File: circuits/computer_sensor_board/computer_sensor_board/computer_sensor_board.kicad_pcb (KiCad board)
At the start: 2 copper layers, 70 x 35 mm, 13 parts, among them J1 Conn_Switching_Hub, J2 Conn_Jetson, J5 Conn_VLP16, J6 Conn_Main_DCDC, J7 Conn_Router

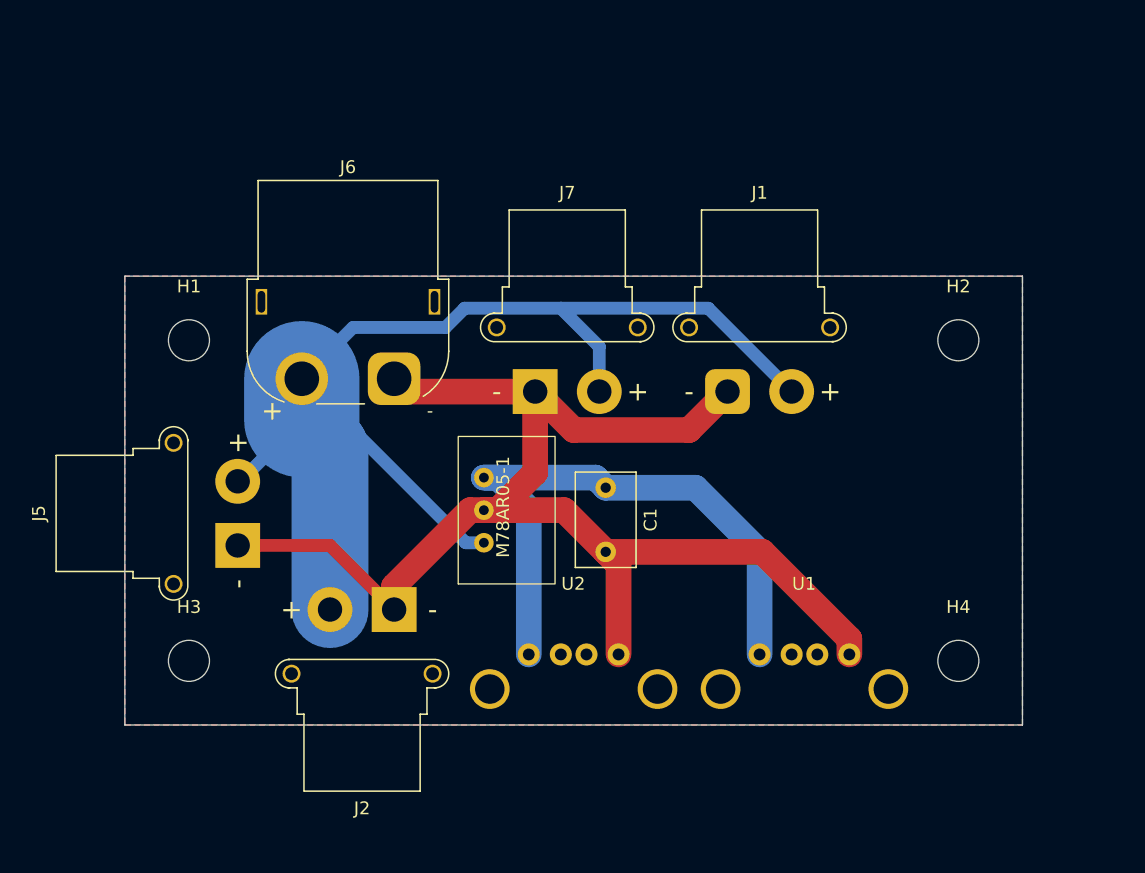
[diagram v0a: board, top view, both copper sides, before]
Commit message: change Pch MOSFET
Signed-off-by: Masaya Kataoka <ms.kataoka@gmail.com>
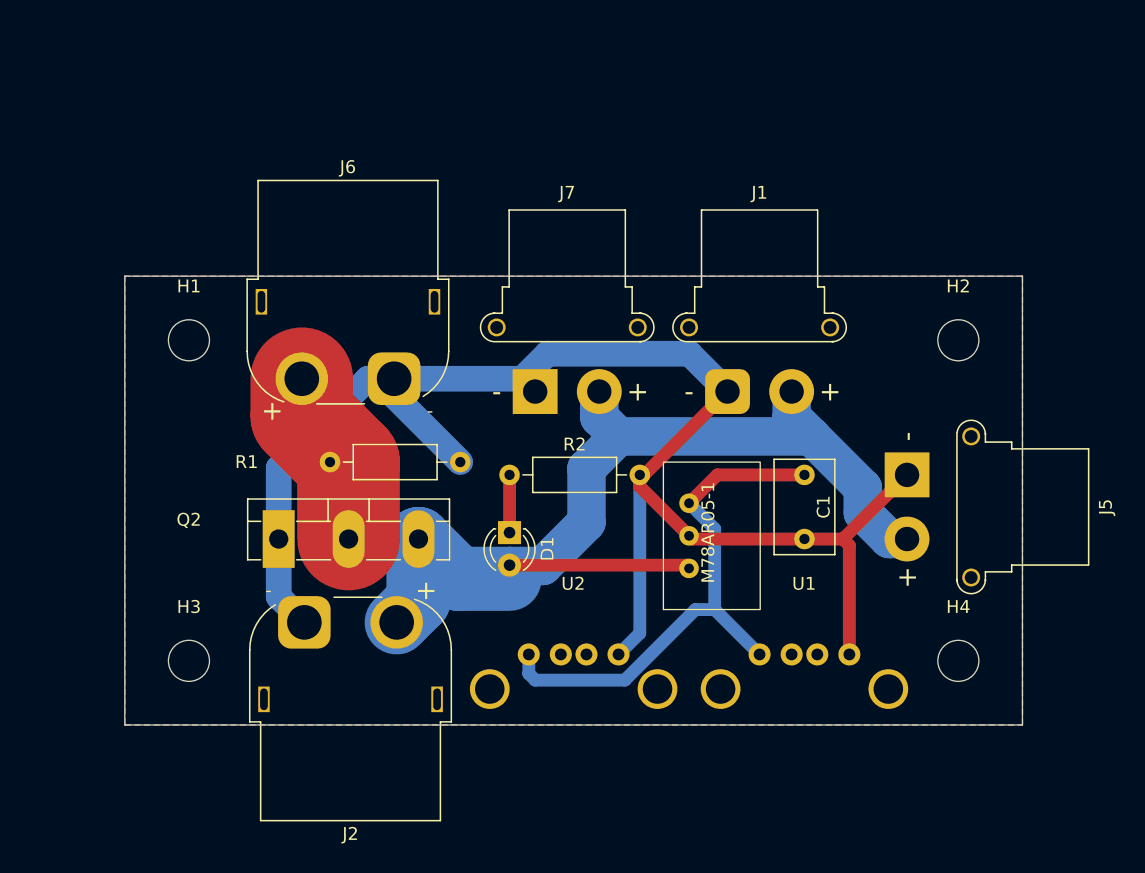
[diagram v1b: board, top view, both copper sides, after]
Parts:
- added D1: LED, LED_THT:LED_D3.0mm, F.Cu at (200.0, 75.0)
- added Q2: 2SJ555-E, Package_TO_SOT_THT:TO-3P-3_Vertical, F.Cu at (182.0, 75.5)
- added R1: 100K, Resistor_THT:R_Axial_DIN0207_L6.3mm_D2.5mm_P10.16mm_Horizontal, F.Cu at (186.0, 69.5)
- added R2: 390, Resistor_THT:R_Axial_DIN0207_L6.3mm_D2.5mm_P10.16mm_Horizontal, F.Cu at (200.0, 70.5)
- J2: footprint Connector_AMASS:AMASS_XT30PW-F_1x02_P2.50mm_Horizontal -> Connector_AMASS:AMASS_XT60PW-F_1x02_P7.20mm_Horizontal
- moved J5 52.5 mm to (231.0, 70.5), turned to -90 degrees
- moved M78AR05-1 16.1 mm to (216.0, 75.0)
- moved C1 15.5 mm to (223.0, 70.5)
- moved J2 7.07 mm to (184.0, 82.0)
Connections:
- J1 pad 2: Net-(J1-Pin_2) -> Net-(D1-A)
- J2 pad 2: Net-(J1-Pin_2) -> Net-(D1-A)
- J5 pad 2: Net-(J1-Pin_2) -> Net-(D1-A)
- J6 pad 2: Net-(J1-Pin_2) -> Net-(J6-Pin_2)
- J7 pad 2: Net-(J1-Pin_2) -> Net-(D1-A)
- M78AR05-1 pad 1: Net-(J1-Pin_2) -> Net-(D1-A)
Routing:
- net Net-(J1-Pin_2): track 96.3 -> 0.00 mm
- net Net-(D1-A): track 0.00 -> 80.0 mm
- net GND: track 108.3 -> 123.5 mm
- net Net-(J6-Pin_2): track 0.00 -> 14.0 mm
- net Net-(M78AR05-1-Vout): track 47.8 -> 42.5 mm
- net Net-(D1-K): track 0.00 -> 4.50 mm

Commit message: add heatsink
Signed-off-by: Masaya Kataoka <ms.kataoka@gmail.com>
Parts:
- added HS1: Heatsink, 16PB017-01025:16PB017-01025, F.Cu at (187.4, 64.2)
- added U3: Heatsink_sheet, 16PB017-01025:TO-3PH, F.Cu at (187.4, 72.3)
- J2: value Conn_Jetson -> Jetson
- J6: value Conn_Main_DCDC -> Main_DCDC
- moved R1 13.7 mm to (197.4, 62.0)
- moved H1 10.0 mm to (175.0, 50.0)
- moved H2 10.0 mm to (235.0, 50.0)
- moved J1 10.0 mm to (217.0, 54.0)
- moved J6 10.0 mm to (191.0, 53.0)
- moved J7 10.0 mm to (202.0, 54.0)
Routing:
- net Net-(D1-A): track 80.0 -> 104.5 mm
- net Net-(J6-Pin_2): track 14.0 -> 34.3 mm
- net GND: track 123.5 -> 126.7 mm
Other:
- board size 70 x 35 mm -> 70 x 45 mm
